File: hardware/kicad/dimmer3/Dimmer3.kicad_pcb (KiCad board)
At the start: 2 copper layers, 64 x 60 mm, 40 parts, among them J100 Stapelstecker 2x20, J101 Kettenstecker, Buchse oben (S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, J102 Kettenstecker, Stift unten (S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, J103 Leistungsstecker, Buchse oben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, J104 Leistungsstecker, Stift unten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, J5 LED-Kanal 1, J6 LED-Kanal 2, J7 LED-Kanal 3, Q1 NCE6050KA, Q10 IRFR5305, Q2 NCE6050KA, Q3 NCE6050KA, U100 STM32C011F6P6, U101 SN74LVC1G175, U102 SN74LVC2G00DCUR, U103 SN74LVC1G08

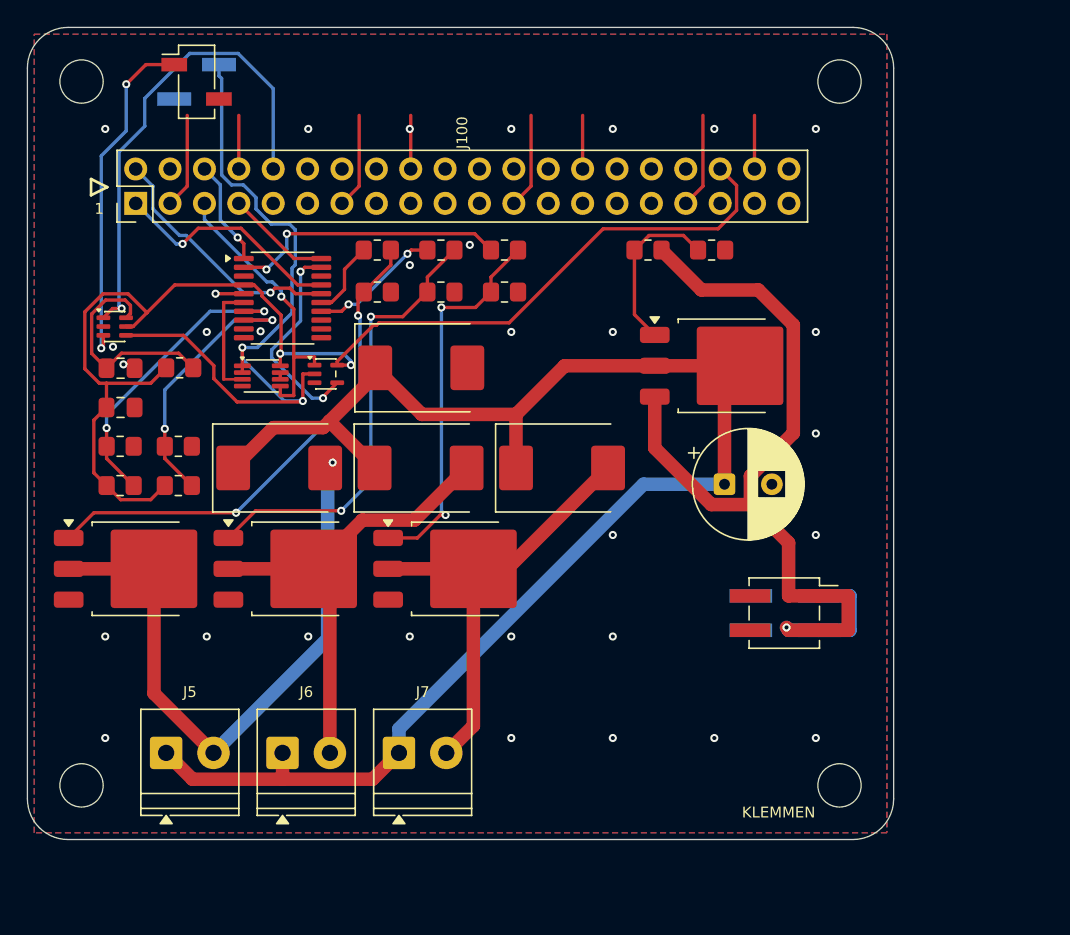
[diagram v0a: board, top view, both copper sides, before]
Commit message: Aufgabe 8b: Dimmer3 verlegt -- 0 Verletzungen, 0 offene Posten
Wurf e3_5 (fuenfter Wurf der zweiten Serie, gebaut aus dem Stand von
e51a338). Kette wie beim Motormodul: bauen -> Vorverdrahtungs-Gate
(0 Verletzungen ohne Router) -> autoroute -> masseheiler -> DRC.

  kicad-cli pcb drc --severity-error --exit-code-violations
    Found 0 violations
    Found 0 unconnected items
  masseheiler --nur-pruefen
    alle Masseflaechen haengen zusammen, nichts zu tun
  steckerprobe spec_dimmer3
    alle elf Zeilen gruen, "Stecker sitzen auf der Vertragslage."
  pcb_checks
    Vias: 76, alle beidseitig angebunden
    ANTENNE_FREI (29.0..50.0 x 42.9..51.9): F.Cu kupferfrei

Der Router liess in diesem Wurf keine einzige Verbindung offen;
masseheiler heilte fuenf Gussfragmente ueber einfache Vias.

Co-Authored-By: Claude Fable 5 <noreply@anthropic.com>
Claude-Session: https://claude.ai/code/session_01KDus95JJwCeRuwccgBWEi5
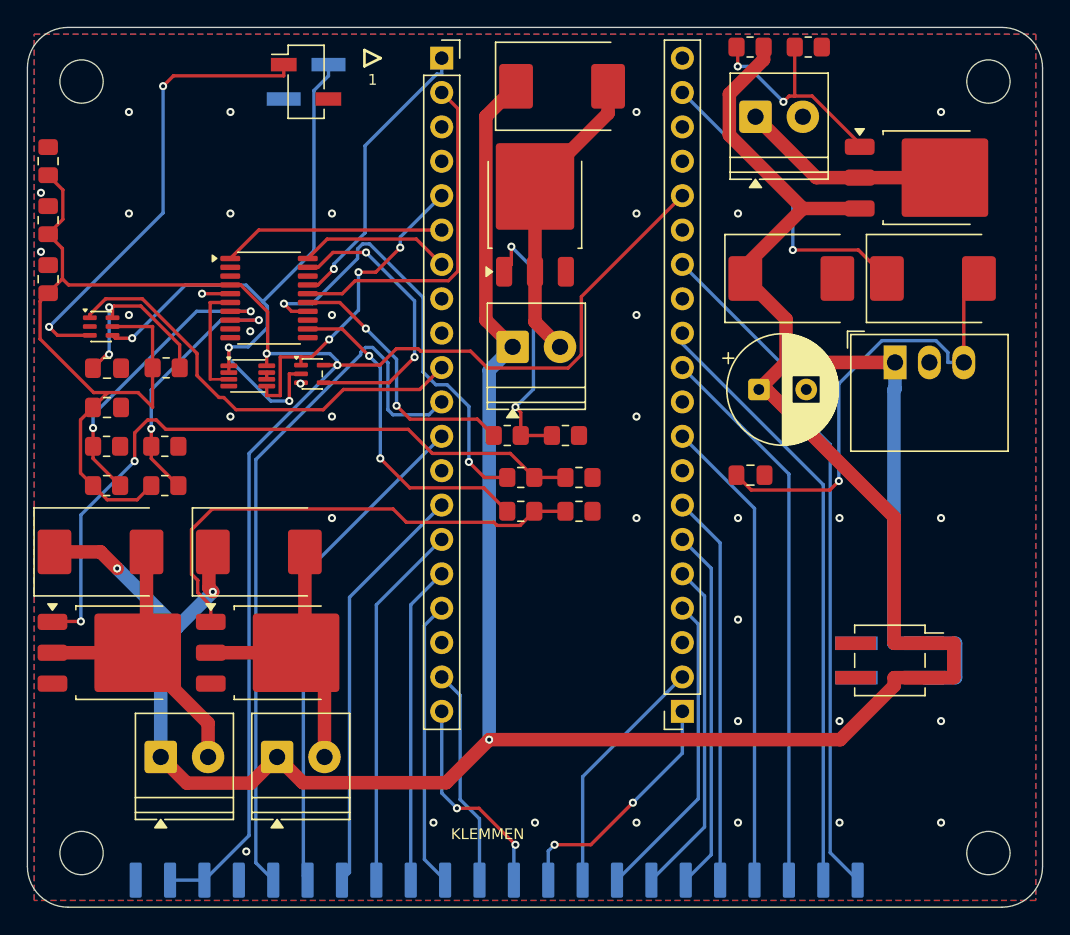
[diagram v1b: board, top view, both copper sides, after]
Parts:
- removed C12: 220u, CP_Radial_D8.0mm_P3.50mm
- removed D10: SMCJ30A, D_SMC
- removed Q10: IRFR5305, TO-252-3_TabPin2
- removed R11, R12: 10k, R_0805_2012Metric_Pad1.20x1.40mm_HandSolder
- added C102: 100n, C_0805_2012Metric_Pad1.18x1.45mm_HandSolder, F.Cu at (1.53, 9.88)
- added C103: 100n, C_0805_2012Metric_Pad1.18x1.45mm_HandSolder, F.Cu at (1.53, 14.2)
- added C104: 100n, C_0805_2012Metric_Pad1.18x1.45mm_HandSolder, F.Cu at (1.53, 18.6)
- added C90: 220u, CP_Radial_D8.0mm_P3.50mm, F.Cu at (54.0, 26.8)
- added C91: 22u, C_0805_2012Metric_Pad1.18x1.45mm_HandSolder, F.Cu at (53.4, 33.1)
- added D90: SMCJ30A, D_SMC, F.Cu at (56.4, 18.6)
- added D91: SS36C, D_SMC, F.Cu at (66.9, 18.6)
- added J105: Stapelstecker rechts, Pico-Pins 21..40 (Buchse), PinSocket_1x20_P2.54mm_Vertical, F.Cu at (48.4, 50.5)
- added J90: Versorgung Eingang, TerminalBlock_Phoenix_PT-1,5-2-3.5-H_1x02_P3.50mm_Horizontal, F.Cu at (53.8, 6.60)
- added J95: Randpads GPIO, unbestueckt (THT-Loetpad), Randpad_Reihe_1x18, B.Cu at (18.2, 63.0)
- added J96: Randpads Versorgung: 2x 3V3 + 2x GND, unbestueckt (THT-Loet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, Randpad_Reihe_1x04, B.Cu at (8.00, 63.0)
- added Q90: IRFR5305, TO-252-3_TabPin2, F.Cu at (66.5, 11.1)
- added R90: 10k, R_0805_2012Metric_Pad1.20x1.40mm_HandSolder, F.Cu at (53.4, 1.45)
- added R91: 10k, R_0805_2012Metric_Pad1.20x1.40mm_HandSolder, F.Cu at (57.7, 1.45)
- added U90: K7805-1000R3, Converter_DCDC_RECOM_R-78B-2.0_THT, F.Cu at (64.1, 24.8)
- D1, D2, D3: value SS36 -> SS36C
- J100: value Stapelstecker 2x20 -> Stapelstecker links, Pico-Pins 1..20 (Buchse); footprint PinHeader_2x20_P2.54mm_Vertical -> PinSocket_1x20_P2.54mm_Vertical
- Q1, Q2, Q3: value NCE6050KA -> NCE6020AK
- moved Q1 39.9 mm to (37.5, 13.0), turned to 90 degrees
- moved J5 39.4 mm to (35.9, 23.6)
- moved D1 35.1 mm to (39.5, 4.35)
- moved J100 25.0 mm to (30.6, 2.27), turned to 0 degrees
- moved D2 24.4 mm to (5.40, 38.8)
- moved D3 23.2 mm to (17.1, 38.8)
- moved RG3 19.3 mm to (36.5, 35.8)
- moved RG2 17.8 mm to (36.5, 33.2)
- moved RP1 17.5 mm to (39.8, 30.1)
- moved RP3 17.1 mm to (40.8, 35.8)
- moved RP2 17.1 mm to (40.8, 33.2)
- moved RG1 16.7 mm to (35.5, 30.1)
- moved Q3 14.5 mm to (18.6, 46.2)
- moved Q2 14.4 mm to (6.89, 46.2)
- moved H4 12.1 mm to (71.0, 61.0)
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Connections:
- J100 pad 11: unconnected-(J100-Pin_11-Pad11) -> /GP8
- J100 pad 12: unconnected-(J100-Pin_12-Pad12) -> /GP9
- J100 pad 14: unconnected-(J100-Pin_14-Pad14) -> /GP10
- J100 pad 15: unconnected-(J100-Pin_15-Pad15) -> /GP11
- J100 pad 16: unconnected-(J100-Pin_16-Pad16) -> /GP12
- J100 pad 17: unconnected-(J100-Pin_17-Pad17) -> /GP13
- J100 pad 19: unconnected-(J100-Pin_19-Pad19) -> /GP14
- J100 pad 20: unconnected-(J100-Pin_20-Pad20) -> /GP15
- J103 pad 1: /PWR24V -> /+24V
- J103 pad 3: /PWR24V -> /+24V
- J104 pad 1: /PWR24V -> /+24V
- J104 pad 3: /PWR24V -> /+24V
- U100 pad 10: /IN2 -> unconnected-(U100-PA3-Pad10)
- U100 pad 11: /NSLEEP -> unconnected-(U100-PA4-Pad11)
- U100 pad 12: /NFAULT -> /PWM3
- U100 pad 13: /IPROPI -> unconnected-(U100-PA6-Pad13)
- U100 pad 2: /PWM3 -> unconnected-(U100-PC14-Pad2)
- U100 pad 9: /IN1 -> unconnected-(U100-PA2-Pad9)
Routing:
- net /+24V: track 115.2 -> 248.6 mm, vias 0 -> 3
- net /PWR24V: track 68.4 -> 0.00 mm, vias 1 -> 0
- net 3V3: track 92.6 -> 152.7 mm
- net /GP8: track 0.00 -> 53.4 mm
- net /GP28: track 0.00 -> 50.9 mm
- net /GP27: track 0.00 -> 44.7 mm
- net GND: track 46.0 -> 2.09 mm, vias 31 -> 36
- net /GP26: track 0.00 -> 41.1 mm
- net /GP9: track 0.00 -> 37.2 mm
- net /GP22: track 0.00 -> 35.0 mm
- net /+5V_LOKAL: track 0.00 -> 33.8 mm, vias 0 -> 1
- net /GP10: track 0.00 -> 30.8 mm
- net /GP21: track 0.00 -> 28.9 mm
- net /GP11: track 0.00 -> 27.2 mm
- net /GP20: track 0.00 -> 26.8 mm
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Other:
- board size 64 x 60 mm -> 75 x 65 mm
